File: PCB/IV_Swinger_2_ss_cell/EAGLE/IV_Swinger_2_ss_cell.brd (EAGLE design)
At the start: 59.7 x 53.3 mm, 34 parts

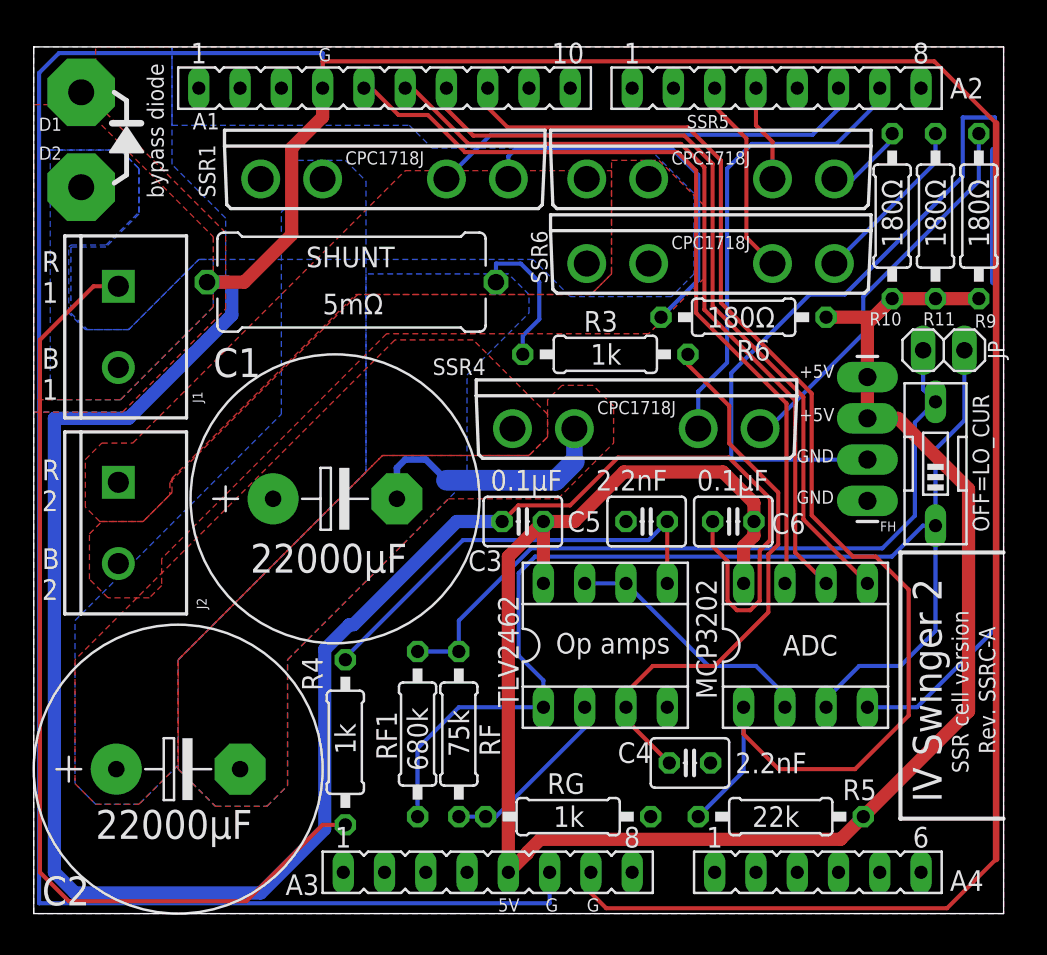
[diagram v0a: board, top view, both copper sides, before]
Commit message: Change SSR4 from lin D1 to D8 on SSR cell version PCB (Issue #49)
This fixes Issue #49 on the SSR cell version PCB. SSR4 is now controlled by Arduino pin D8. This is now RevB (or SSRC-B) of this PCB.

This commit includes:
   EAGLE files, .sch and .brd
   Zip of the Rev_B Gerber files
   PDFs of the modified schematic, and the modified top and bottom images
   Updated GIFs that compare the SSR cell version with the other variants
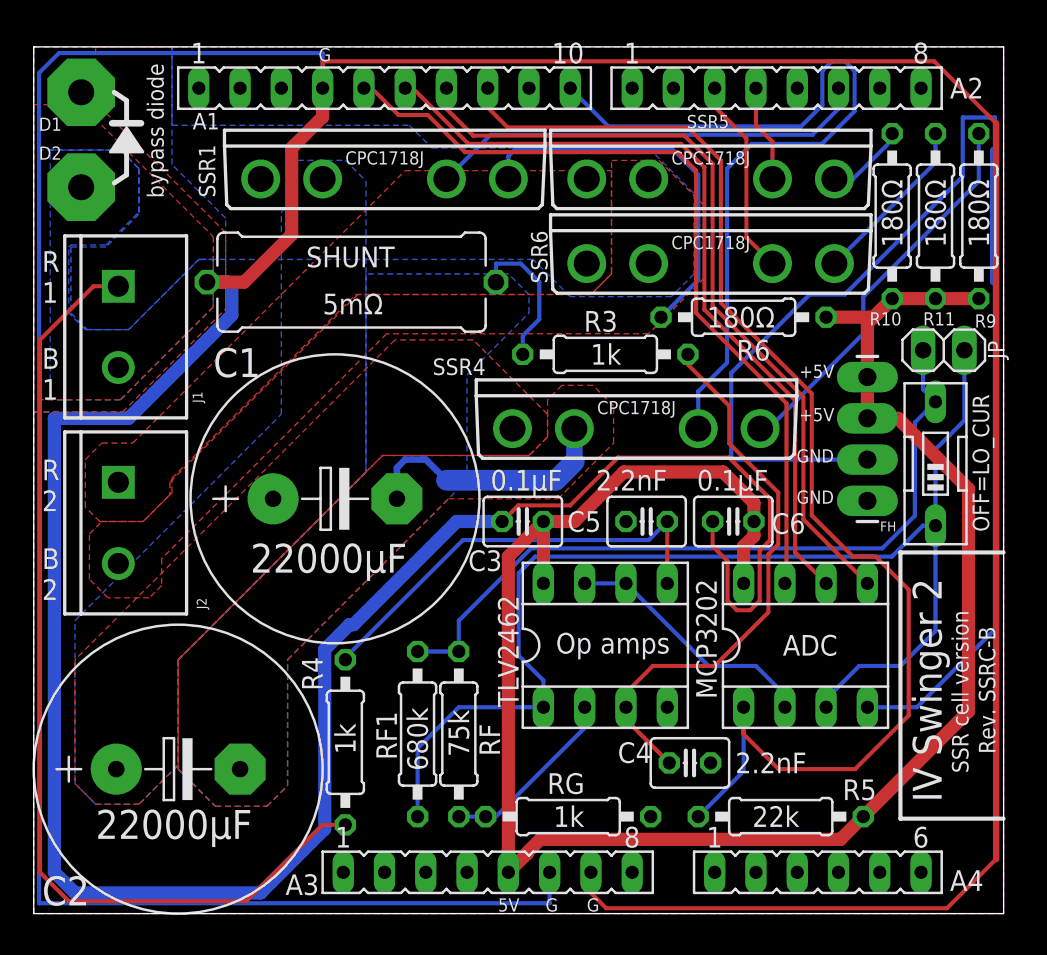
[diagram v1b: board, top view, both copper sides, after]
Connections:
- net N20: now also A1.10; no longer A2.7
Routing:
- net N20: track 28.6 -> 50.2 mm
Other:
- board text added: "Rev. SSRC-B"
- board text removed: "Rev. SSRC-A"
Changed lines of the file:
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@@
 <text x="55.88" y="6.858" size="1.778" layer="21" rot="R90">IV Swinger 2</text>
 <text x="57.531" y="8.645396875" size="1.016" layer="21" rot="R90">SSR cell version</text>
-<text x="59.182" y="9.83046875" size="1.016" layer="21" rot="R90">Rev. SSRC-A</text>
+<text x="59.182" y="9.83046875" size="1.016" layer="21" rot="R90">Rev. SSRC-B</text>
 <text x="17.526" y="52.451" size="0.8128" layer="21">G</text>
 <wire x1="6.604" y1="48.641" x2="4.826" y2="48.641" width="0.4064" layer="21"/>
@@
 <text x="19.812" y="11.684" size="1.27" layer="22" rot="MR270">1k</text>
 <text x="45.72" y="36.068" size="1.27" layer="22" rot="MR0">180Ω</text>
-<circle x="52.07" y="50.8" radius="1.524" width="0.3048" layer="22"/>
+<circle x="33.02" y="50.8" radius="1.524" width="0.3048" layer="22"/>
 </plain>
 <attributes>
@@
 <signal name="N20">
 <contactref element="SSR4" pad="3"/>
+<contactref element="A1" pad="10"/>
+<wire x1="33.02" y1="50.8" x2="35.3822" y2="48.4378" width="0.254" layer="16"/>
+<wire x1="35.3822" y1="48.4378" x2="47.211375" y2="48.4378" width="0.254" layer="16"/>
+<wire x1="48.5394" y1="51.870725" x2="49.119675" y2="52.451" width="0.254" layer="16"/>
+<wire x1="49.119675" y1="52.451" x2="49.940325" y2="52.451" width="0.254" layer="16"/>
+<wire x1="49.940325" y1="52.451" x2="50.5206" y2="51.870725" width="0.254" layer="16"/>
+<wire x1="47.211375" y1="48.4378" x2="48.5394" y2="49.765825" width="0.254" layer="16"/>
+<wire x1="48.5394" y1="49.765825" x2="48.5394" y2="51.870725" width="0.254" layer="16"/>
+<wire x1="50.5206" y1="51.870725" x2="50.5206" y2="49.3776" width="0.254" layer="16"/>
+<wire x1="50.5206" y1="49.3776" x2="48.514" y2="47.371" width="0.254" layer="16"/>
+<wire x1="48.514" y1="47.371" x2="44.196" y2="47.371" width="0.254" layer="16"/>
+<wire x1="44.196" y1="47.371" x2="42.672" y2="45.847" width="0.254" layer="16"/>
+<wire x1="42.672" y1="45.847" x2="42.672" y2="33.909" width="0.254" layer="16"/>
 <wire x1="42.672" y1="33.909" x2="40.894" y2="32.131" width="0.254" layer="16"/>
-<wire x1="40.894" y1="29.845" x2="40.894" y2="32.131" width="0.254" layer="16"/>
-<contactref element="A2" pad="7"/>
-<wire x1="52.07" y1="50.8" x2="52.07" y2="50.038" width="0.254" layer="16"/>
-<wire x1="52.07" y1="50.038" x2="49.403" y2="47.371" width="0.254" layer="16"/>
-<wire x1="44.196" y1="47.371" x2="42.672" y2="45.847" width="0.254" layer="16"/>
-<wire x1="49.403" y1="47.371" x2="44.196" y2="47.371" width="0.254" layer="16"/>
-<wire x1="42.672" y1="45.847" x2="42.672" y2="33.909" width="0.254" layer="16"/>
+<wire x1="40.894" y1="32.131" x2="40.894" y2="29.845" width="0.254" layer="16"/>
 </signal>
 <signal name="N23">
